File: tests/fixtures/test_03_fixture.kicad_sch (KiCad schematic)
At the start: 3 parts, among them J1 Conn_01x01, SW1 Val, SW2 Val

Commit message: Migrate test fixtures from Footprint to LocLoad custom field
Move component location and electrical load encoding from overloaded
Footprint field to new custom LocLoad field. Remove leading pipe
character from encoding format.

Changes:
- Clear Footprint field values (restore to empty string)
- Add LocLoad custom property with format: (FS,WL,BL){S|L|R|G}<value>
- Remove leading | character from encoding format
- Add test_06 fixture files for new test cases

All fixtures now use LocLoad field as single source of component data.

🤖 Generated with [Claude Code](https://claude.com/claude-code)

Co-Authored-By: Claude <noreply@anthropic.com>
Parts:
- J1: LocLoad (none) -> (20,0,0)S10
- SW1: LocLoad (none) -> (0,0,0)R20
- SW2: LocLoad (none) -> (0,1,0)R20
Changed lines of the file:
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@@
+			)
+		)
+		(property "LocLoad" "(0,1,0)R20"
+			(at 119.38 105.41 0)
+			(effects
+				(font
+					(size 1.27 1.27)
+				)
+				(hide yes)
 			)
 		)
@@
 			)
 		)
+		(property "LocLoad" "(0,0,0)R20"
+			(at 119.38 76.2 0)
+			(effects
+				(font
+					(size 1.27 1.27)
+				)
+				(hide yes)
+			)
+		)
 		(pin "1"
 		)
@@
 			(at 149.86 86.36 0)
 			(effects
+				(font
+					(size 1.27 1.27)
+				)
+				(hide yes)
+			)
+		)
+		(property "LocLoad" "(20,0,0)S10"
+			(at 149.86 86.36 0)
+			(effects

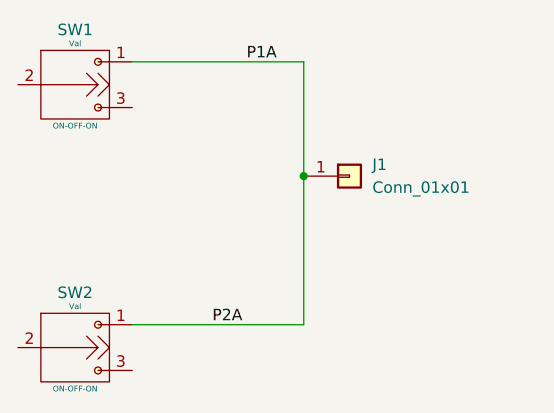
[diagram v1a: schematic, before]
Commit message: Fix multipoint power symbol bug and add diagram enhancements
Bug Fixes:
- Fix multipoint connections with power symbols (GND, +12V, etc.)
  Power symbols now correctly treated as common pin in multipoint
  groups since all components connect to same global net
- Fix UnboundLocalError when components missing LocLoad data
  Wire length calculation now handles missing component coordinates
  gracefully with fallback to default length
- Fix overly aggressive cross-connection filter hiding legitimate
  multipoint wires in component diagrams

New Features:
- Add --2d flag to generate 2D diagrams (FS/BL only) instead of
  default 3D projection with WL axis
- Add component value and description to component diagram titles
  (e.g., "CB1: 30A - Circuit Breaker")

Enhancements:
- Update DEFAULT_WL_SCALE from 3.0 to 1.5 for better 3D projection
- Update diagram tests for independent X/Y scaling (scale_x, scale_y)
- Update wire label position to return axis name ('BL', 'FS', 'WL')

Test Updates:
- All 265 tests passing
- Update test fixtures (test_03, test_08)
- Add test_09_fixture for additional test coverage
- Remove obsolete test_07_fixture.csv

File Cleanup:
- Archive parser_netlist_ARCHIVED.py to docs/archive/

🤖 Generated with [Claude Code](https://claude.com/claude-code)

Co-Authored-By: Claude <noreply@anthropic.com>
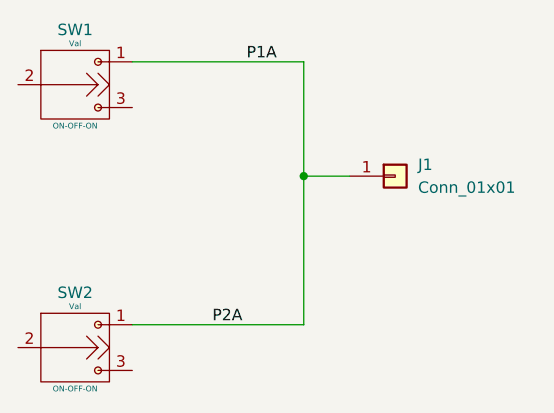
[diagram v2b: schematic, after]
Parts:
- SW2: LocLoad (0,1,0)R20 -> (0,1,2)R20
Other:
- moved on the sheet: J1
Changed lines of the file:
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@@
+		)
+	)
+	(wire
+		(pts
+			(xy 149.86 86.36) (xy 144.78 86.36)
+		)
+		(stroke
+			(width 0)
+			(type default)
 		)
 	)
@@
 			)
 		)
-		(property "LocLoad" "(0,1,0)R20"
+		(property "LocLoad" "(0,1,2)R20"
 			(at 119.38 105.41 0)
 			(effects
@@
 	(symbol
 		(lib_id "Connector_Generic:Conn_01x01")
-		(at 149.86 86.36 0)
+		(at 154.94 86.36 0)
 		(unit 1)
 		(exclude_from_sim no)
@@
 		(fields_autoplaced yes)
 		(property "Reference" "J1"
-			(at 152.4 85.0899 0)
+			(at 157.48 85.0899 0)
 			(effects
 				(font
@@
 		)
 		(property "Value" "Conn_01x01"
-			(at 152.4 87.6299 0)
+			(at 157.48 87.6299 0)
 			(effects
 				(font
@@
 		)
 		(property "Footprint" ""
-			(at 149.86 86.36 0)
+			(at 154.94 86.36 0)
 			(effects
 				(font
@@
 		)
 		(property "Datasheet" "~"
-			(at 149.86 86.36 0)
+			(at 154.94 86.36 0)
 			(effects
 				(font
@@
 		)
 		(property "Description" "Generic connector, single row, 01x01, script generated (kicad-library-utils/schlib/autogen/connector/)"
-			(at 149.86 86.36 0)
+			(at 154.94 86.36 0)
 			(effects
 				(font
@@
 		)
 		(property "LocLoad" "(20,0,0)S10"
-			(at 149.86 86.36 0)
-			(effects
-				(font
+			(at 154.94 86.36 0)
+			(effects
+				(font
